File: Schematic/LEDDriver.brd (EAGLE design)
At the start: 43.1 x 48.2 mm, 32 parts, among them IC1 LM324N, IC2 LM317, IC3 75176AP, IC4 LM317

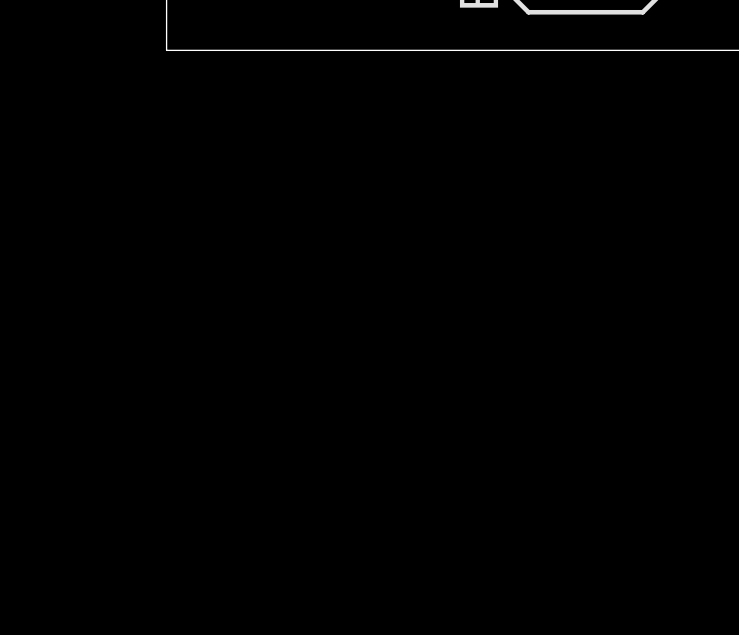
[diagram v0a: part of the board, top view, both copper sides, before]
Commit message: Add pull downs to enable pins of LEDs to not flash up the LEDs on boot time
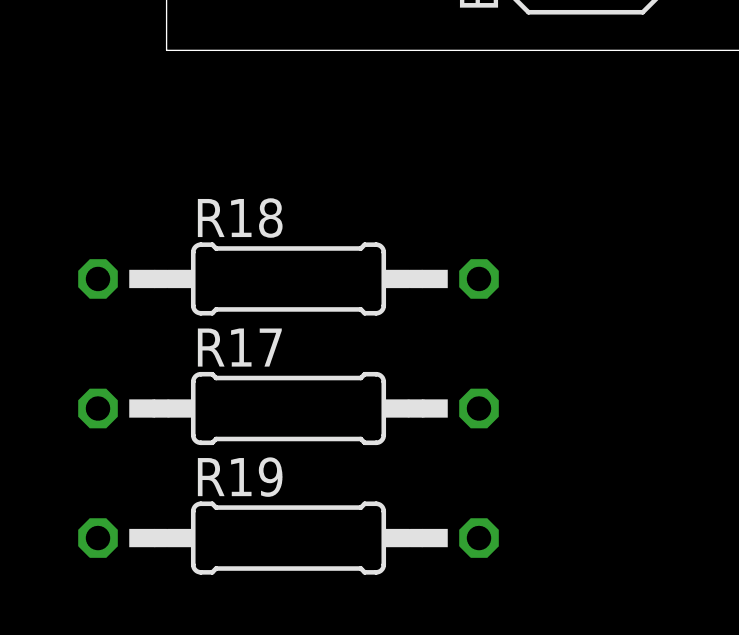
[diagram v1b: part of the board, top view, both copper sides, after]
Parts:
- added R17, R18, R19: 50k, rcl:0207/12
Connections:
- net GND: now also R17.1, R18.1, R19.1
- net GPIO0: now also R18.2
- net GPIO2: now also R17.2
- net GPIO3: now also R19.2
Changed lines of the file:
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@@
 <element name="R15" library="rcl" package="0204V" value="240" x="7.62" y="36.83" rot="R90"/>
 <element name="R16" library="rcl" package="0207/10" value="720" x="10.16" y="33.02" rot="R180"/>
+<element name="R18" library="rcl" package="0207/12" value="50k" x="4.064" y="-7.62"/>
+<element name="R17" library="rcl" package="0207/12" value="50k" x="4.064" y="-11.938"/>
+<element name="R19" library="rcl" package="0207/12" value="50k" x="4.064" y="-16.256"/>
 </elements>
 <signals>
@@
 <wire x1="20.32" y1="38.1" x2="20.32" y2="35.56" width="0.4064" layer="16"/>
 <wire x1="25.4" y1="38.1" x2="25.4" y2="35.56" width="0.4064" layer="16"/>
+<contactref element="R19" pad="1"/>
+<contactref element="R17" pad="1"/>
+<contactref element="R18" pad="1"/>
 <wire x1="35.56" y1="35.56" x2="40.64" y2="48.26" width="0" layer="19" extent="1-1"/>
 <wire x1="17.78" y1="35.56" x2="20.32" y2="35.56" width="0" layer="19" extent="16-16"/>
@@
 <wire x1="15.24" y1="17.78" x2="15.24" y2="15.24" width="0" layer="19" extent="1-1"/>
 <wire x1="0" y1="5.08" x2="15.24" y2="10.16" width="0" layer="19" extent="1-1"/>
+<wire x1="-2.286" y1="-7.62" x2="0" y2="5.08" width="0" layer="19" extent="1-1"/>
+<wire x1="-2.286" y1="-11.938" x2="-2.286" y2="-7.62" width="0" layer="19" extent="1-1"/>
+<wire x1="-2.286" y1="-16.256" x2="-2.286" y2="-11.938" width="0" layer="19" extent="1-1"/>
 </signal>
 <signal name="N$5">
@@
 <contactref element="ESP8266" pad="5"/>
 <contactref element="XL6009_EN" pad="2"/>
+<contactref element="R17" pad="2"/>
 <wire x1="15.24" y1="7.62" x2="43.18" y2="7.62" width="0" layer="19" extent="1-1"/>
+<wire x1="10.414" y1="-11.938" x2="15.24" y2="7.62" width="0" layer="19" extent="1-1"/>
 </signal>
 <signal name="GPIO0">
 <contactref element="ESP8266" pad="3"/>
 <contactref element="XL6009_EN" pad="1"/>
+<contactref element="R18" pad="2"/>
 <wire x1="15.24" y1="5.08" x2="43.18" y2="10.16" width="0" layer="19" extent="1-1"/>
+<wire x1="10.414" y1="-7.62" x2="15.24" y2="5.08" width="0" layer="19" extent="1-1"/>
 </signal>
 <signal name="GPIO3">
 <contactref element="ESP8266" pad="1"/>
 <contactref element="XL6009_EN" pad="3"/>
+<contactref element="R19" pad="2"/>
 <wire x1="15.24" y1="2.54" x2="43.18" y2="5.08" width="0" layer="19" extent="1-1"/>
+<wire x1="10.414" y1="-16.256" x2="15.24" y2="2.54" width="0" layer="19" extent="1-1"/>
 </signal>
 <signal name="N$3">

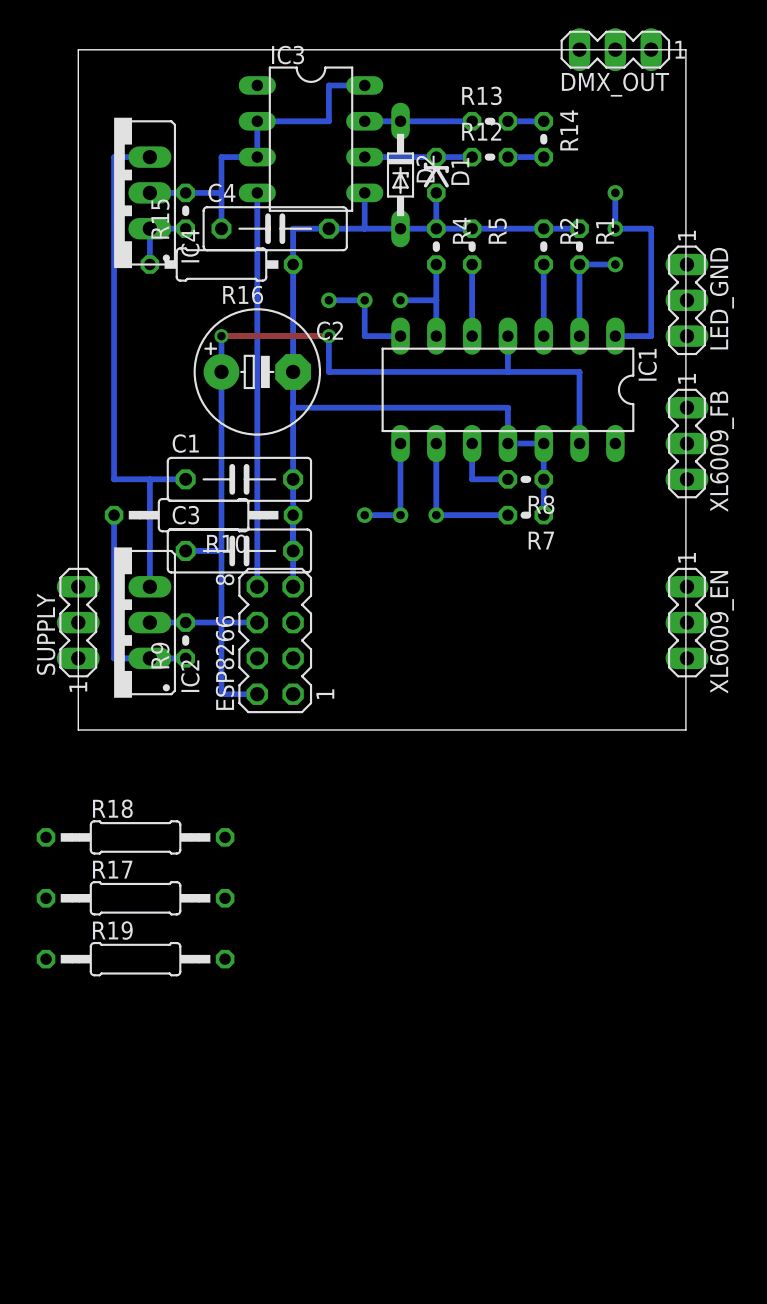
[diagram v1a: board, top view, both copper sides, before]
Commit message: Switch OpAmp of, if all LEDs are off
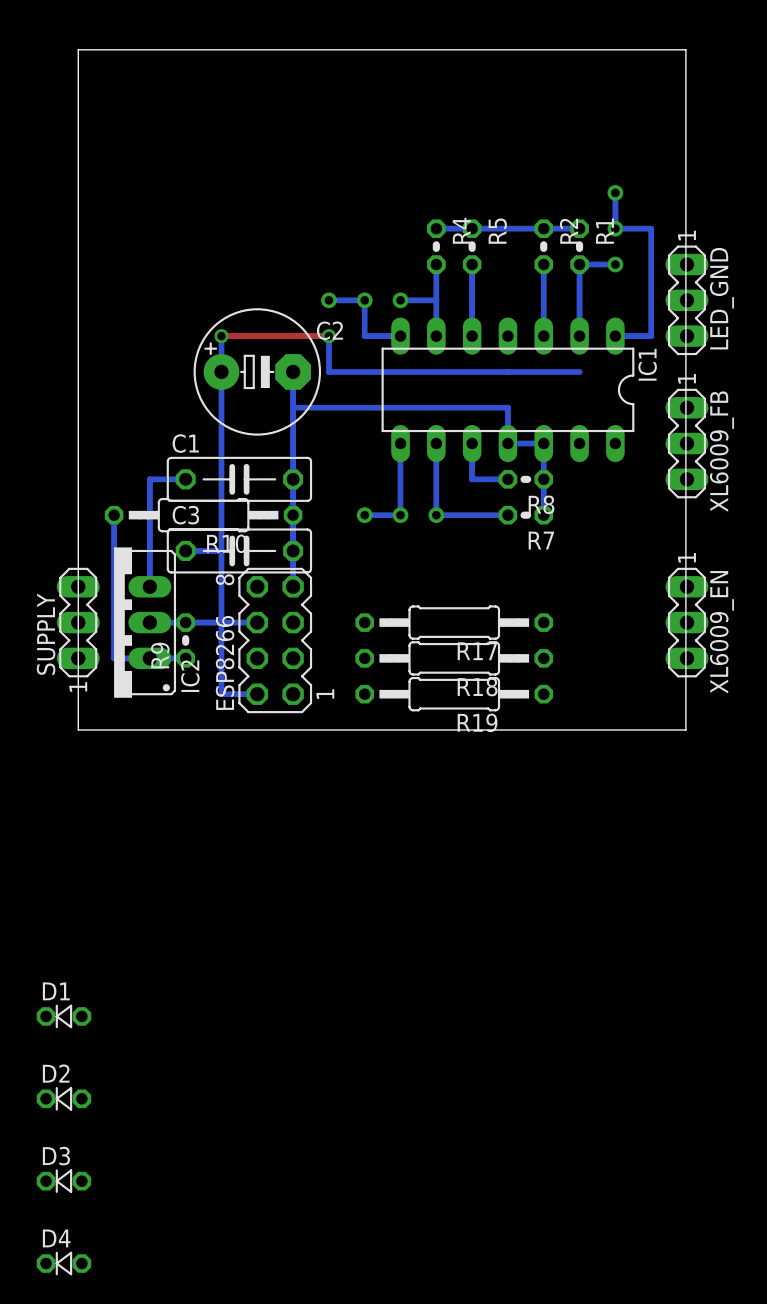
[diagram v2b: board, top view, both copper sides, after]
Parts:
- removed C4: 100n, rcl:C075-032X103
- removed DMX_OUT: (no value), con-lstb:MA03-1
- removed IC3: 75176AP, 751xx:DIL08
- removed IC4: LM317, v-reg:317TS
- removed R12, R13: 22, rcl:0204V
- removed R14: 120, rcl:0204V
- removed R15: 240, rcl:0204V
- removed R16: 720, rcl:0207/10
- added D3, D4: 1N4148, diode:D-2.5
- D1: value (none) -> 1N4148; device diode:ZDIO-2.5 -> diode:D-2.5
- D2: value (none) -> 1N4148; device diode:DO34Z7 -> diode:D-2.5
- moved D2 69.7 mm to (-1.02, -26.2), turned to 0 degrees
- moved D1 65.3 mm to (-1.02, -20.3), turned to 0 degrees
- moved R17 29.9 mm to (26.7, 7.62), turned to 180 degrees
- moved R19 29.4 mm to (26.7, 2.54), turned to 180 degrees
- moved R18 25.9 mm to (26.7, 5.08), turned to 180 degrees
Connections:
- removed net +5V: C4.1, IC3.2, IC3.3, IC3.8, IC4.2, R15.2
- removed net DMX2: DMX_OUT.2, R12.2, R14.2
- removed net N$1: ESP8266.8, IC3.4
- removed net N$14: D1.C, IC3.6, R12.1
- removed net N$15: D2.C, IC3.7, R13.1
- removed net N$16: DMX_OUT.3, R13.2, R14.1
- removed net N$8: IC4.1, R15.1, R16.2
- new net N$23: D4.A, ESP8266.8
- new net VDD: D1.C, D2.C, D3.C, D4.C, IC1.13, IC1.4
- net +12V: no longer IC4.3
- net +3V3: no longer IC1.13, IC1.4
- net GND: no longer C4.2, D1.A, D2.A, DMX_OUT.1, IC3.5, R16.1
- net GPIO0: now also D2.A
- net GPIO2: now also D3.A
- net GPIO3: now also D1.A
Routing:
- net N$1: track 27.9 -> 0.00 mm
- net +12V: track 38.1 -> 10.2 mm
- net +5V: track 25.4 -> 0.00 mm
- net GND: track 78.7 -> 53.3 mm
- net N$15: track 7.62 -> 0.00 mm
- net N$14: track 7.62 -> 0.00 mm
- net +3V3: track 73.7 -> 66.0 mm
- net N$8: track 5.08 -> 0.00 mm
- net N$16: track 2.54 -> 0.00 mm
- net DMX2: track 2.54 -> 0.00 mm
